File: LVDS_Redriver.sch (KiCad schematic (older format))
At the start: 14 parts, among them U4 DS25BR440_RTA_40

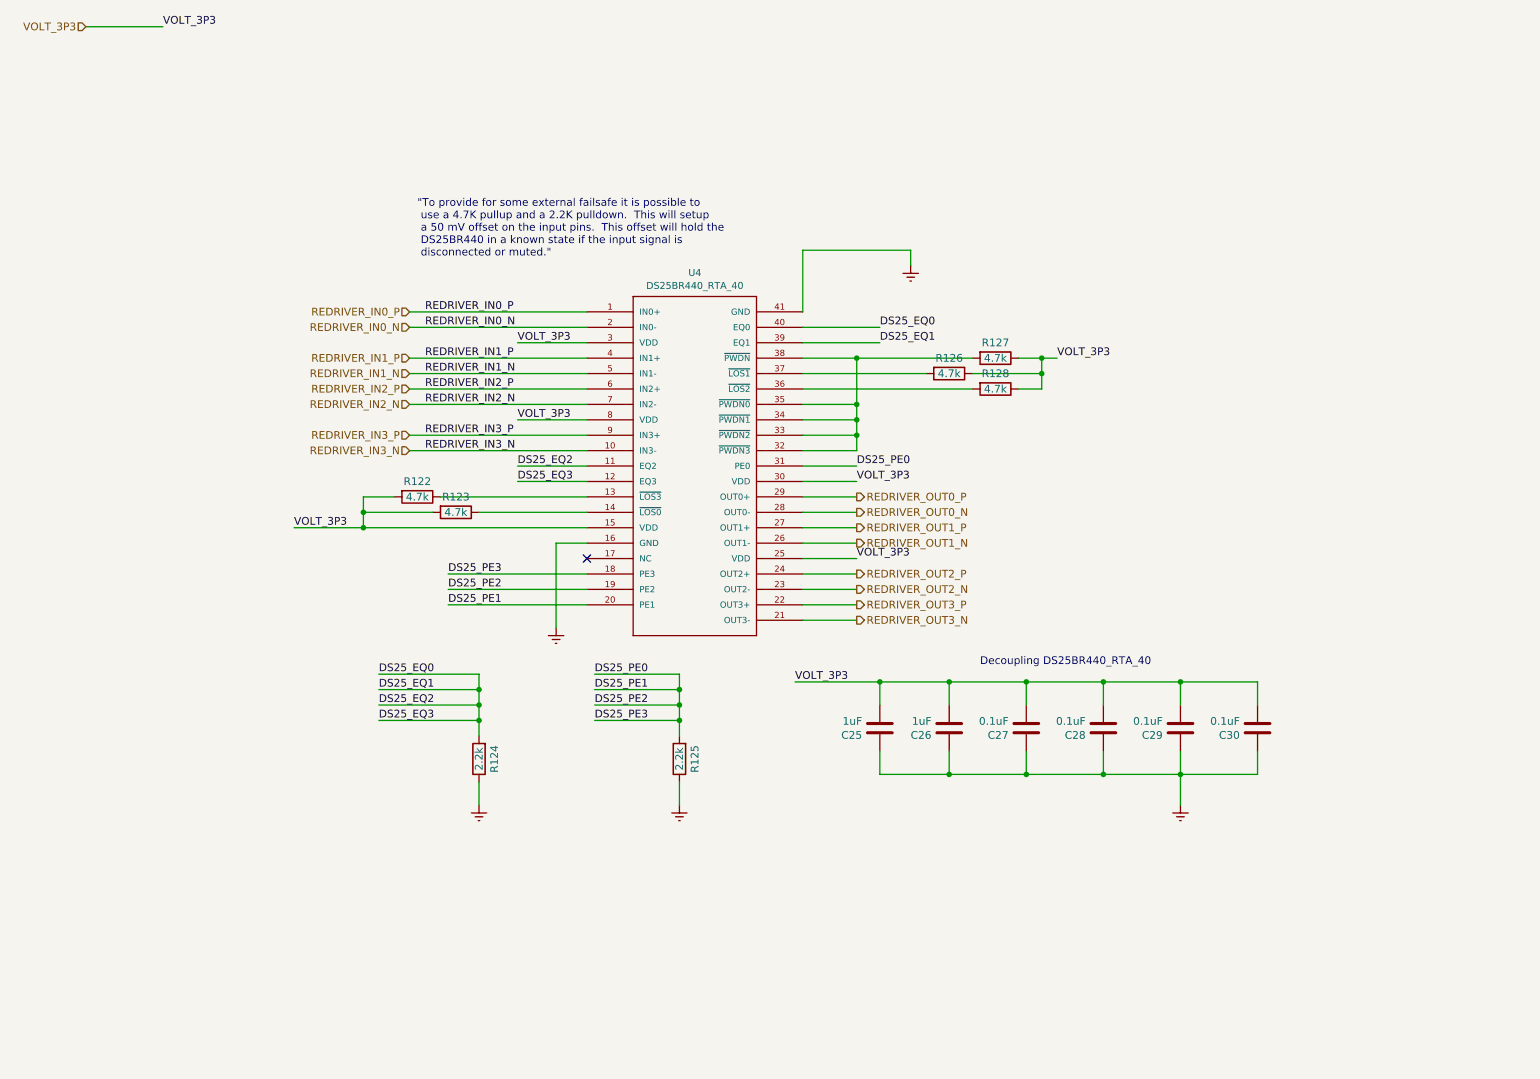
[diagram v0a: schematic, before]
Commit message: good, added re-driver
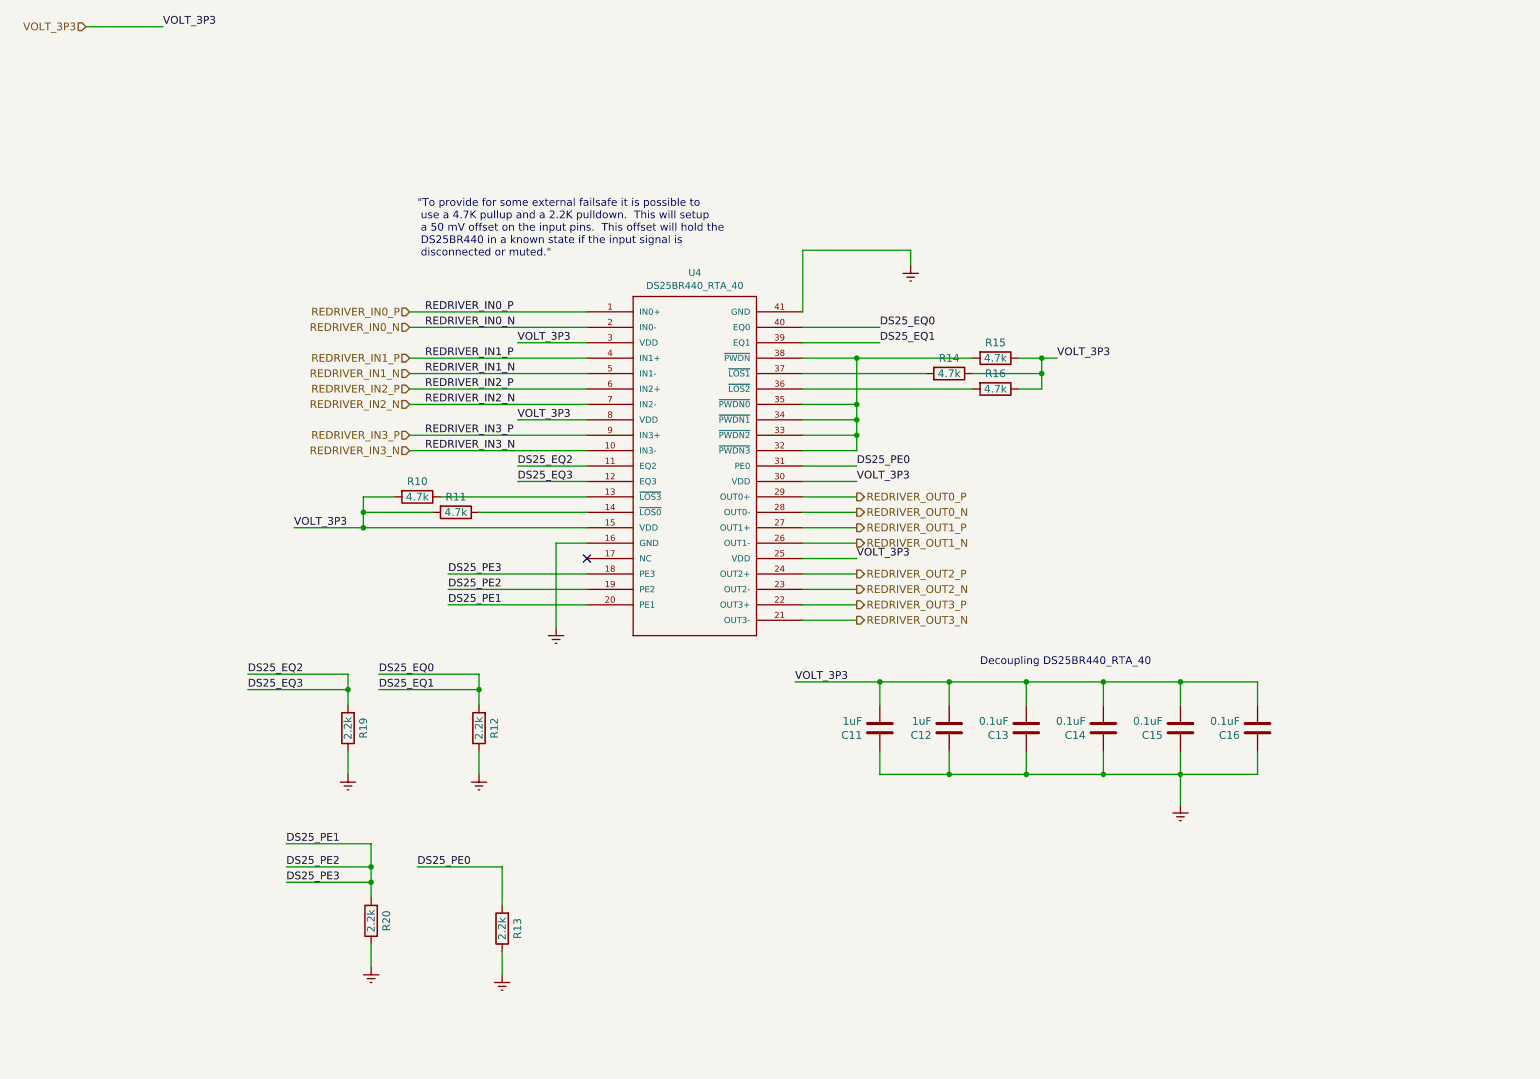
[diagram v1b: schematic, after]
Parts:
- added R17, R18: 2.2k, Resistors_SMD:R_0805, symbol FMC_MIPI_v2:R
- renumbered C30 to C10, C25 to C5, C26 to C6, C27 to C7, C28 to C8, C29 to C9, R122 to R3, R123 to R4, R124 to R5, R125 to R6, R126 to R7, R127 to R8, R128 to R9, U4 to U3
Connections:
- net DS25_EQ0: no longer U3.11 (EQ2), U3.12 (EQ3)
- net DS25_PE0: no longer U3.18 (PE3), U3.19 (PE2), U3.20 (PE1)
- net Earth: now also R17.1, R18.1
- new net DS25_EQ2: R17.2, U3.11 (EQ2), U3.12 (EQ3)
- new net DS25_PE1: R18.2, U3.18 (PE3), U3.19 (PE2), U3.20 (PE1)
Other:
- moved on the sheet: R12, R13

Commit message: good, before reducing
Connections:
- net REDRIVER_OUT1_N: no longer U3.26 (OUT1-)
- net REDRIVER_OUT1_P: no longer U3.27 (OUT1+)
- net REDRIVER_OUT2_N: no longer U3.23 (OUT2-)
- net REDRIVER_OUT2_P: no longer U3.24 (OUT2+)
- net REDRIVER_OUT3_N: no longer U3.21 (OUT3-)
- net REDRIVER_OUT3_P: no longer U3.22 (OUT3+)
- new net sheet61CC513F/LVDS_IN_N: U3.26 (OUT1-)
- new net sheet61CC513F/LVDS_IN_P: U3.27 (OUT1+)
- new net sheet61CC9F81/LVDS_IN_N: U3.23 (OUT2-)
- new net sheet61CC9F81/LVDS_IN_P: U3.24 (OUT2+)
- new net sheet61CCEEAC/LVDS_IN_N: U3.21 (OUT3-)
- new net sheet61CCEEAC/LVDS_IN_P: U3.22 (OUT3+)
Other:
- moved on the sheet: C10, C5, C6, C7, C8, C9, R17, R18, R5, R6

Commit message: before re-arranging
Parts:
- renumbered C7 to C10, C8 to C11, C9 to C12, C10 to C13, C5 to C8, C6 to C9, R8 to R10, R9 to R11, R17 to R3, R18 to R4, R3 to R7, R4 to R8, R7 to R9, U3 to U4
